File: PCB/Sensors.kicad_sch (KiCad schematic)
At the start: 11 parts, among them U401 MMC5633NJL, U402 LSM6DSV320, U403 MS5607-02BA, U404 SAM-M8Q

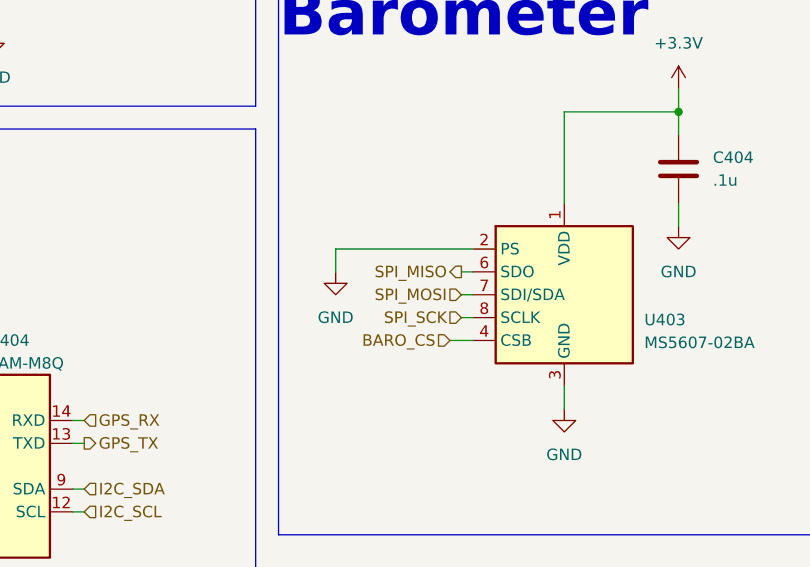
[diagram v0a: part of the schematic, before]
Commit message: Fixed barometer wiring
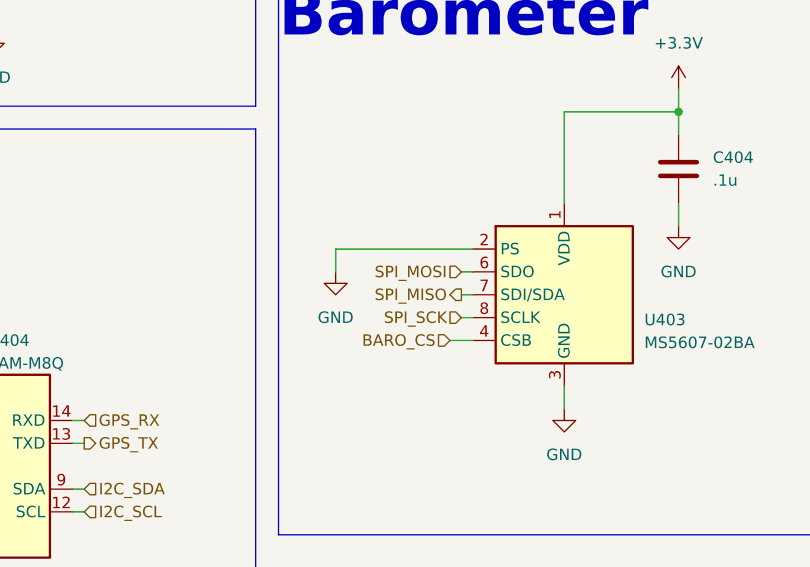
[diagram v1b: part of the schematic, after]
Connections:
- net SPI_MISO: now also U403.7 (SDI/SDA); no longer U403.6 (SDO)
- net SPI_MOSI: now also U403.6 (SDO); no longer U403.7 (SDI/SDA)
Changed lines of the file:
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@@
 	(hierarchical_label "SPI_MOSI"
 		(shape input)
-		(at 121.92 105.41 180)
+		(at 121.92 102.87 180)
 		(effects
 			(font
@@
 	(hierarchical_label "SPI_MISO"
 		(shape output)
-		(at 121.92 102.87 180)
+		(at 121.92 105.41 180)
 		(effects
 			(font

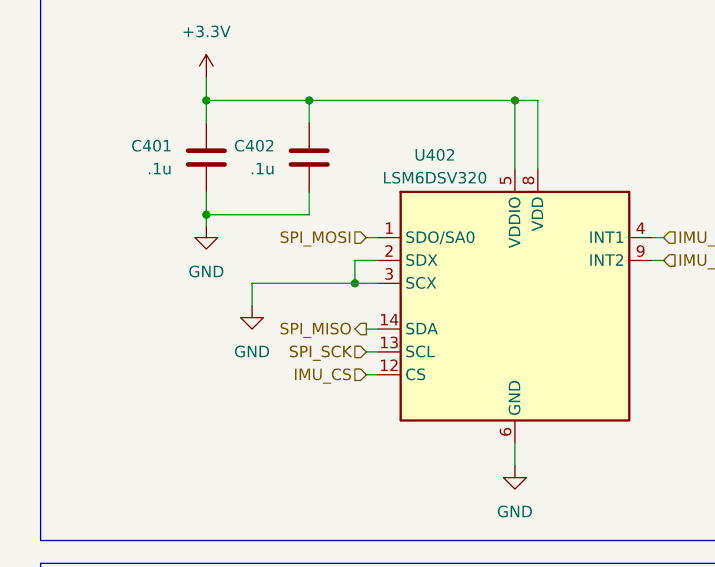
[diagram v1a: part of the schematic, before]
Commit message: Flipped MOSI and MISO on the IMU
Updated all output files for the PCB
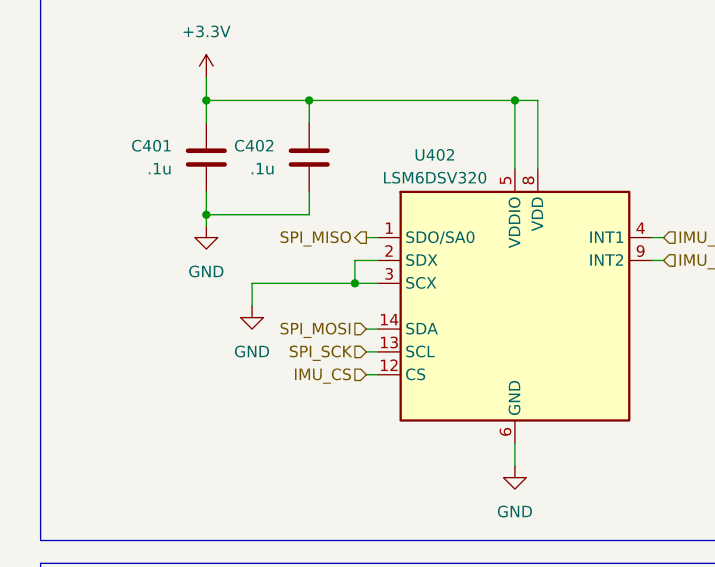
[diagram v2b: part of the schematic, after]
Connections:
- net SPI_MISO: now also U402.1 (SDO/SA0); no longer U402.14 (SDA)
- net SPI_MOSI: now also U402.14 (SDA); no longer U402.1 (SDO/SA0)
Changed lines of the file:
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@@
 	(hierarchical_label "SPI_MOSI"
 		(shape input)
-		(at 53.34 50.8 180)
+		(at 53.34 60.96 180)
 		(effects
 			(font
@@
 	(hierarchical_label "SPI_MISO"
 		(shape output)
-		(at 53.34 60.96 180)
+		(at 53.34 50.8 180)
 		(effects
 			(font

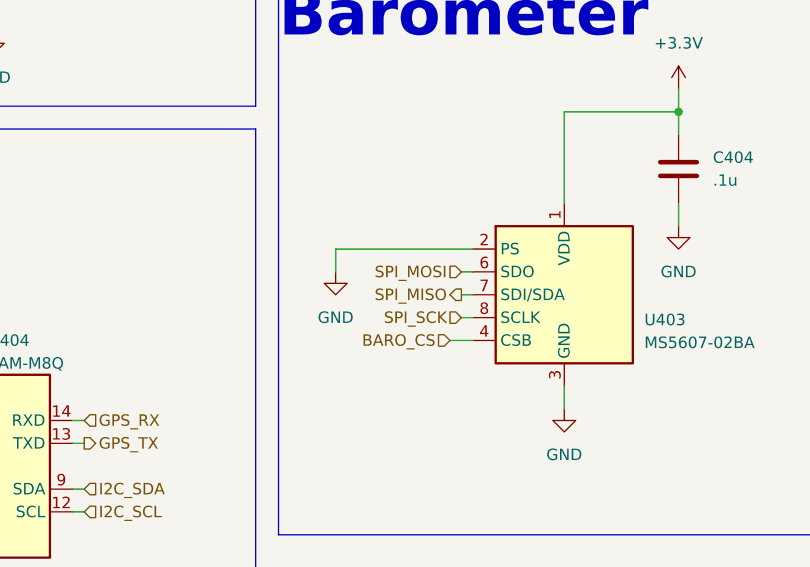
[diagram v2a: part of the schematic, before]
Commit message: Update Barometer SPI connection
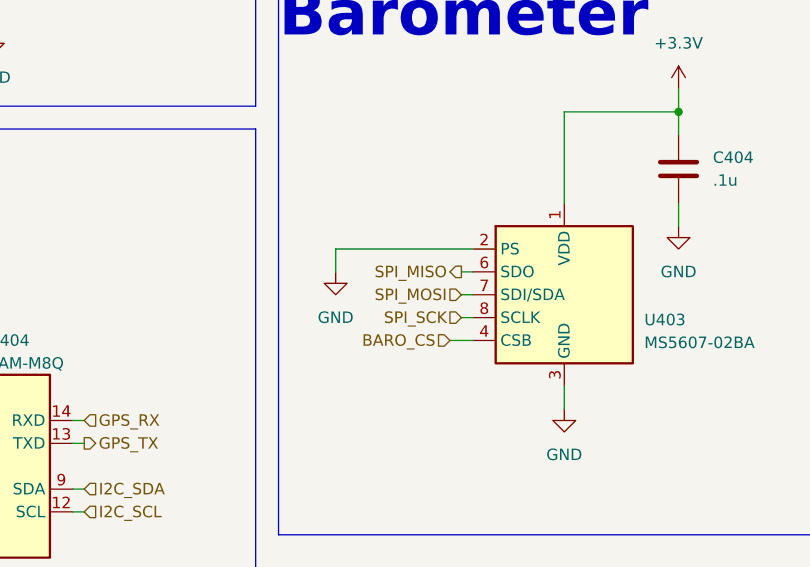
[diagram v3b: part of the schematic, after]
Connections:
- net SPI_MISO: now also U403.6 (SDO); no longer U403.7 (SDI/SDA)
- net SPI_MOSI: now also U403.7 (SDI/SDA); no longer U403.6 (SDO)
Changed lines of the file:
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@@
 	(hierarchical_label "SPI_MOSI"
 		(shape input)
-		(at 121.92 102.87 180)
+		(at 121.92 105.41 180)
 		(effects
 			(font
@@
 	(hierarchical_label "SPI_MISO"
 		(shape output)
-		(at 121.92 105.41 180)
+		(at 121.92 102.87 180)
 		(effects
 			(font

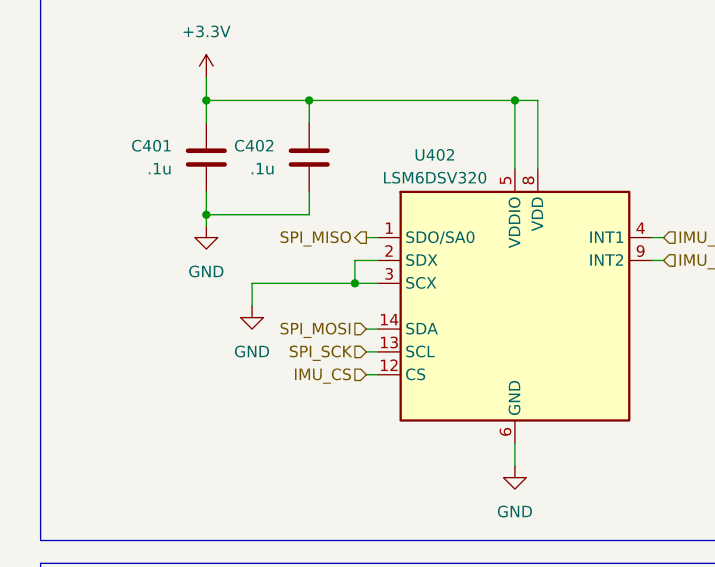
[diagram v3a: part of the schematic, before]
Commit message: Added basic buzzer, LED, and fiducials to the schematic
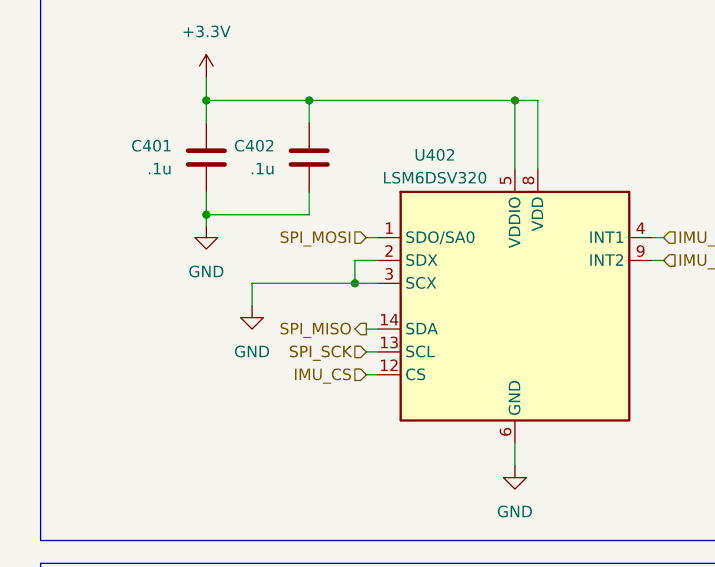
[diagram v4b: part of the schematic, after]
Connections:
- net SPI_MISO: now also U402.14 (SDA); no longer U402.1 (SDO/SA0)
- net SPI_MOSI: now also U402.1 (SDO/SA0); no longer U402.14 (SDA)
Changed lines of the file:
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@@
 	(hierarchical_label "SPI_MOSI"
 		(shape input)
-		(at 53.34 60.96 180)
+		(at 53.34 50.8 180)
 		(effects
 			(font
@@
 	(hierarchical_label "SPI_MISO"
 		(shape output)
-		(at 53.34 50.8 180)
+		(at 53.34 60.96 180)
 		(effects
 			(font
